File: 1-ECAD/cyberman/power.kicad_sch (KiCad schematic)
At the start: 49 parts, among them J601 S3B-ZR-SM4A-TF, U601 MAX17048G+T10, U602 BQ25896RTWR, U604 RS3221-3.3YF3, U605 DMN313DLT-7, U606 DMP1045U-7, U607 TPS62825DMQR, U608 TPS62824ADMQ, U609 MMDT2907A-7-F

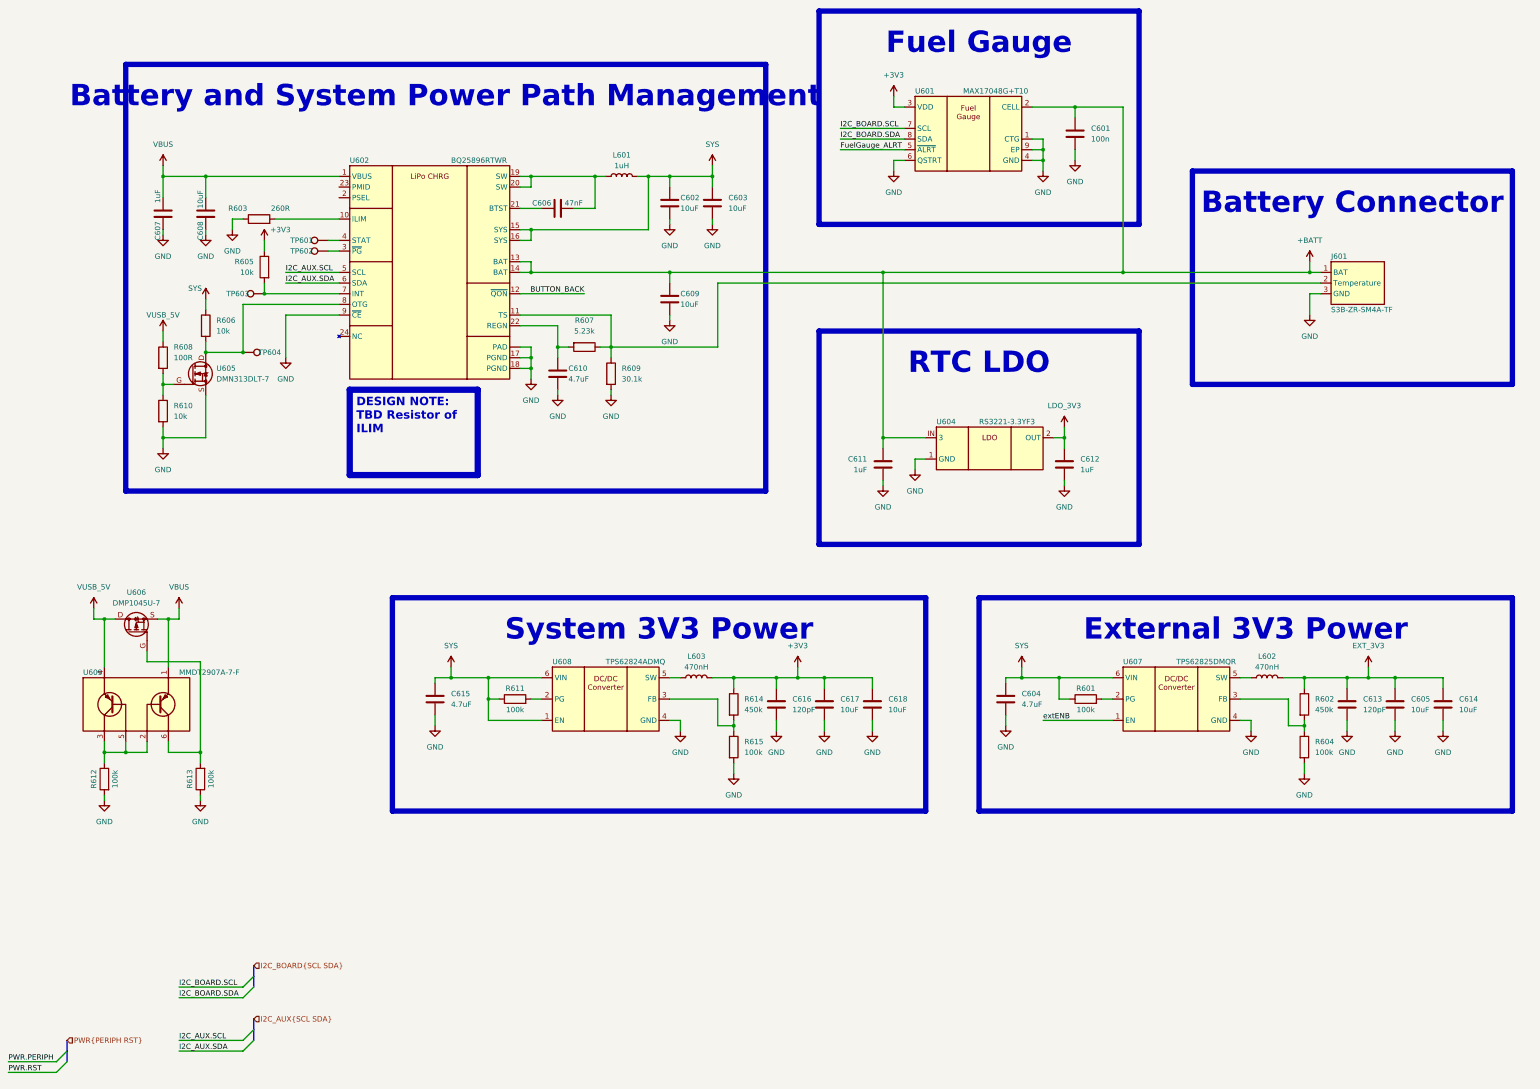
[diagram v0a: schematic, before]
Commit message: power page almost done
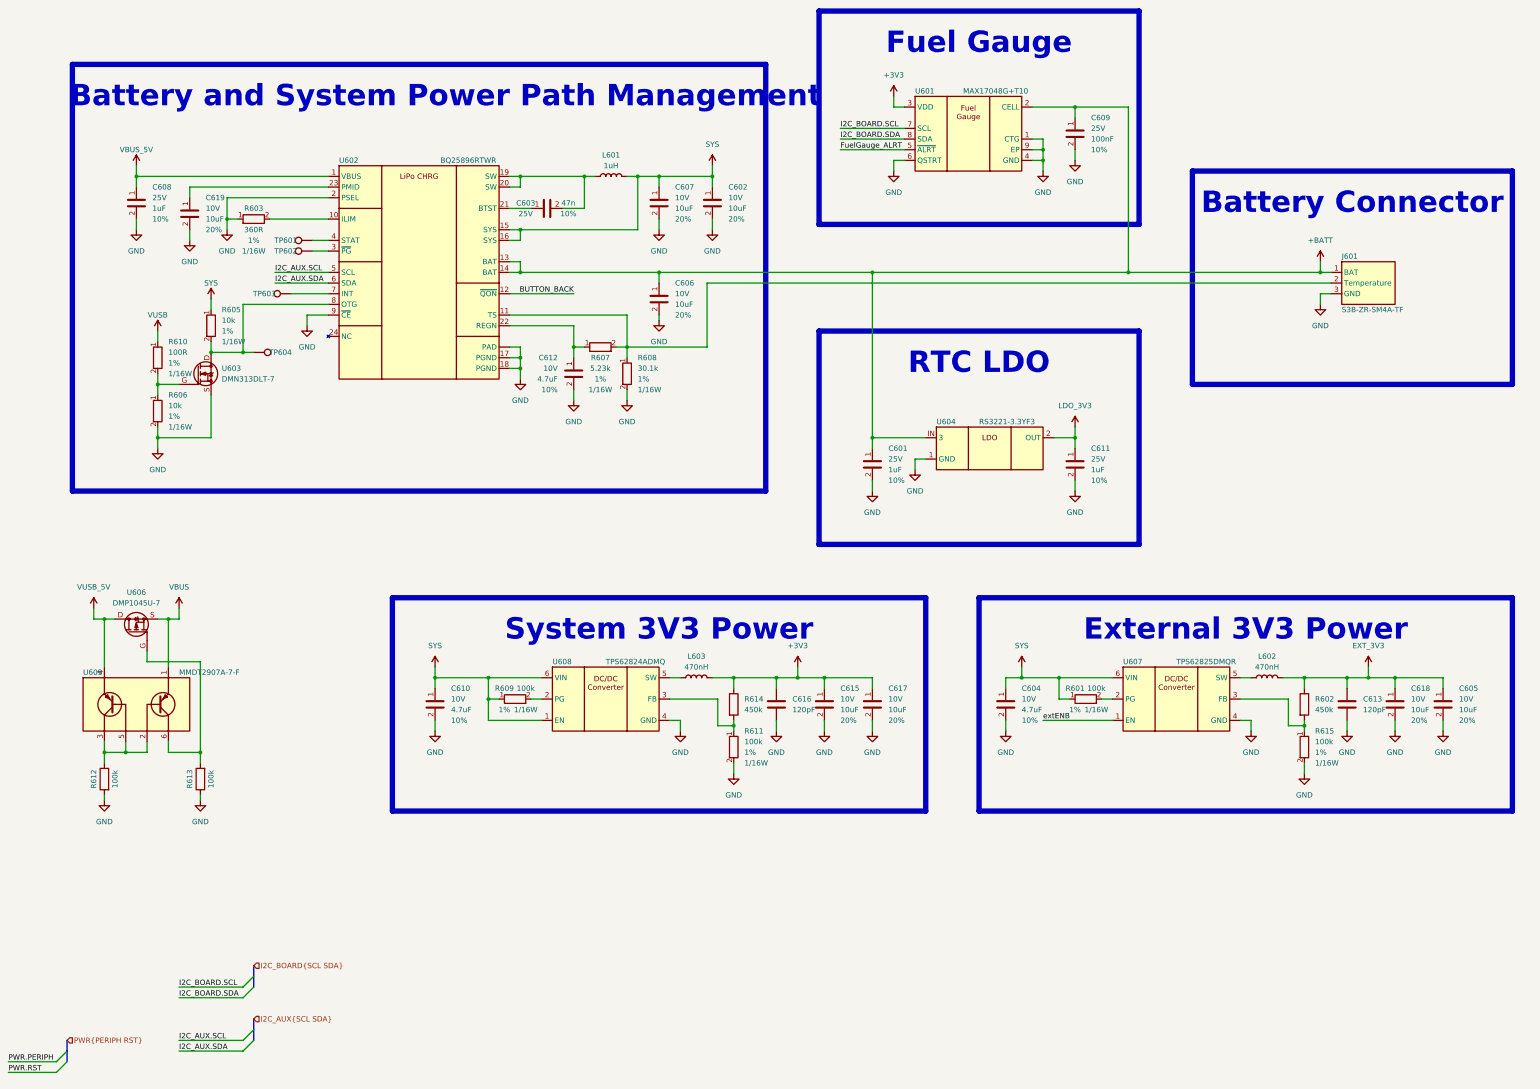
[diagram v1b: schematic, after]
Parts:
- removed C601: 100n, symbol Device:C
- removed C602, C603, C605, C608, C609, C614, C617, C618: 10uF, symbol Device:C
- removed C604, C610, C615: 4.7uF, symbol Device:C
- removed C606: 47nF, symbol Device:C
- removed C607, C611, C612: 1uF, symbol Device:C
- removed R601, R604, R611, R615: 100k, symbol Device:R
- removed R603: 260R, symbol Device:R
- removed R605, R606, R610: 10k, symbol Device:R
- removed R607: 5.23k, symbol Device:R
- removed R608: 100R, symbol Device:R
- removed R609: 30.1k, symbol Device:R
- removed U605: DMN313DLT-7, symbol 0_CI_smd:DMN313DLT-7
- added C601, C608, C611: CC0402KRX5R8BB105, 0_capacitor_smd:C_0402, symbol 0_capacitor_smd:CC0402KRX5R8BB105
- added C602, C605, C606, C607, C615, C617, C618, C619: CC0402MRX5R6BB106, 0_capacitor_smd:C_0402, symbol 0_capacitor_smd:CC0402MRX5R6BB106
- added C603: CC0402KRX7R8BB473, 0_capacitor_smd:C_0402, symbol 0_capacitor_smd:CC0402KRX7R8BB473
- added C604, C610, C612: CC0402KRX5R6BB475, 0_capacitor_smd:C_0402, symbol 0_capacitor_smd:CC0402KRX5R6BB475
- added C609: CC0402KRX7R8BB104, 0_capacitor_smd:C_0402, symbol 0_capacitor_smd:CC0402KRX7R8BB104
- added R601, R609, R611, R615: RC0402FR-07100KL, 0_resistor_smd:R_0402, symbol 0_resistor_smd:RC0402FR-07100KL
- added R603: RC0402FR-07360RL, 0_resistor_smd:R_0402, symbol 0_resistor_smd:RC0402FR-07360RL
- added R605, R606: RC0402FR-0710KL, 0_resistor_smd:R_0402, symbol 0_resistor_smd:RC0402FR-0710KL
- added R607: RC0402FR-075K23L, 0_resistor_smd:R_0402, symbol 0_resistor_smd:RC0402FR-075K23L
- added R608: RC0402FR-0730K1L, 0_resistor_smd:R_0402, symbol 0_resistor_smd:RC0402FR-0730K1L
- added R610: RC0402FR-07100RL, 0_resistor_smd:R_0402, symbol 0_resistor_smd:RC0402FR-07100RL
- added U603: DMN313DLT-7, 0_CI_smd:DMN313DLT-7, symbol 0_CI_smd:DMN313DLT-7
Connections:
- net +3V3: now also C615.1, C617.1
- net +BATT: now also C601.1, C606.1, C609.1
- net EXT_3V3: now also C605.1, C618.1
- net GND: now also U602.2 (PSEL), C601.2, C602.2, C604.2, C605.2, C606.2, C607.2, C608.2, C609.2, C610.2, C611.2, C612.2, C615.2, C617.2, C618.2, C619.2, R603.1, R606.2, R608.2, R611.2, R615.2, U603.S
- net LDO_3V3: now also C611.1
- net SYS: now also C602.1, C604.1, C607.1, C610.1, R601.1, R605.1, R609.1
- net VBUS: no longer U602.1 (VBUS)
- net at U602.10 (ILIM): now also R603.2
- net at J601.2 (Temperature), U602.11 (TS): now also R607.2, R608.1
- net at L601.1, U602.19 (SW), U602.20 (SW): now also C603.2
- net at U602.21 (BTST): now also C603.1
- net at U602.22 (REGN): now also C612.1, R607.1
- net at U602.23 (PMID): now also C619.1
- net at TP604.1, U602.8 (OTG): now also R605.2, U603.D
- net at R602.2, U607.3 (FB): now also R615.1
- net at U607.2 (PG): now also R601.2
- net at R614.2, U608.3 (FB): now also R611.1
- net at U608.2 (PG): now also R609.2
- new net: R606.1, R610.2, U603.G
- new net VBUS_5V: C608.1, U602.1 (VBUS)
- new net VUSB: R610.1
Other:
- moved on the sheet: J601, L601, TP601, TP602, TP603, TP604, U602

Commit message: new footprints
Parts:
- removed C613, C616: 120pF, symbol Device:C
- removed R602, R614: 450k, symbol Device:R
- added C614, C616: CC0402KRX7R9BB121, 0_capacitor_smd:C_0402, symbol 0_capacitor_smd:CC0402KRX7R9BB121
- added R604, R614: RC0402FR-07453KL, 0_resistor_smd:R_0402, symbol 0_resistor_smd:RC0402FR-07453KL
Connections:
- net +3V3: now also C614.1, R604.1
- net EXT_3V3: now also C616.1, R614.1
- net GND: now also C614.2, C616.2
- net at R615.1, U607.3 (FB): now also R614.2
- net at R611.1, U608.3 (FB): now also R604.2

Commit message: power page close
siuuuuuuuuuuuu
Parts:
- removed L601: 1uH, symbol Device:L
- removed L602, L603: 470nH, symbol Device:L
- removed R603: RC0402FR-07360RL, 0_resistor_smd:R_0402, symbol 0_resistor_smd:RC0402FR-07360RL
- removed R612, R613: 100k, symbol Device:R
- removed TP601, TP602, TP603, TP604: TestPoint, symbol Connector:TestPoint
- removed U606: DMP1045U-7, symbol 0_CI_smd:DMP1045U-7
- removed U609: MMDT2907A-7-F, 0_CI_smd:MMDT2907A-7-F, symbol 0_CI_smd:MMDT2907A-7-F
- added L601: DFE252012P-1R0M=P2, 0_inductor_smd:DFE252012P-1R0M=P2, symbol 0_inductor_smd:DFE252012P-1R0M=P2
- added L602: MLP2012HR47MT0S1, 0_inductor_smd:MLP2012HR47MT0S1, symbol 0_inductor_smd:MLP2012HR47MT0S1
- added L603: LQM2MPNR47MGHL, 0_inductor_smd:LQM2MPNR47MGHL, symbol 0_inductor_smd:LQM2MPNR47MGHL
- added R601: RC0402FR-07470RL, 0_resistor_smd:R_0402, symbol 0_resistor_smd:RC0402FR-07470RL
- added R602, R613: RC0402FR-0710KL, 0_resistor_smd:R_0402, symbol 0_resistor_smd:RC0402FR-0710KL
- added R615, R616: RC0402FR-07100KL, 0_resistor_smd:R_0402, symbol 0_resistor_smd:RC0402FR-07100KL
- added TP601: STAT, 0_testpoint:TestPoint_Pad_D0.5mm_Front, symbol 0_test_points:testpoint
- added TP602: PG, 0_testpoint:TestPoint_Pad_D0.5mm_Front, symbol 0_test_points:testpoint
- added TP603: TEMP, 0_testpoint:TestPoint_Pad_D0.5mm_Front, symbol 0_test_points:testpoint
- added TP604: OTG, 0_testpoint:TestPoint_Pad_D0.5mm_Front, symbol 0_test_points:testpoint
- added TP605, TP607: 5V1, 0_testpoint:TestPoint_Pad_D0.5mm_Front, symbol 0_test_points:testpoint
- added TP606: 3V31, 0_testpoint:TestPoint_Pad_D0.5mm_Front, symbol 0_test_points:testpoint
- added TP608: 3V32, 0_testpoint:TestPoint_Pad_D0.5mm_Front, symbol 0_test_points:testpoint
- added TP609: GND1, 0_testpoint:TestPoint_Pad_D0.5mm_Front, symbol 0_test_points:testpoint
- added TP610: GND2, 0_testpoint:TestPoint_Pad_D0.5mm_Front, symbol 0_test_points:testpoint
- added TP611: GND3, 0_testpoint:TestPoint_Pad_D0.5mm_Front, symbol 0_test_points:testpoint
- added TP612: BAT1, 0_testpoint:TestPoint_Pad_D0.5mm_Front, symbol 0_test_points:testpoint
- added TP613: EXT3V31, 0_testpoint:TestPoint_Pad_D0.5mm_Front, symbol 0_test_points:testpoint
- added TP614: GND4, 0_testpoint:TestPoint_Pad_D0.5mm_Front, symbol 0_test_points:testpoint
- added TP615: BAT2, 0_testpoint:TestPoint_Pad_D0.5mm_Front, symbol 0_test_points:testpoint
- added TP616: EXT3V32, 0_testpoint:TestPoint_Pad_D0.5mm_Front, symbol 0_test_points:testpoint
- added TP617: SYS1, 0_testpoint:TestPoint_Pad_D0.5mm_Front, symbol 0_test_points:testpoint
- added TP618: LDO1, 0_testpoint:TestPoint_Pad_D0.5mm_Front, symbol 0_test_points:testpoint
- added TP619: SYS2, 0_testpoint:TestPoint_Pad_D0.5mm_Front, symbol 0_test_points:testpoint
- added TP620: LDO2, 0_testpoint:TestPoint_Pad_D0.5mm_Front, symbol 0_test_points:testpoint
- added U607: DMP1045U-7, 0_CI_smd:DMP1045U-7, symbol 0_CI_smd:DMP1045U-7
- added U608: MMDT2907A-7-F, 0_CI_smd:MMDT2907A-7-F, symbol 0_CI_smd:MMDT2907A-7-F
- renumbered C609 to C601, C608 to C602, C607 to C603, C602 to C604, C603 to C605, C619 to C606, C606 to C607, C612 to C608, C601 to C609, C611 to C610, C610 to C611, C614 to C612, C615 to C613, C617 to C614, C604 to C615, C618 to C617, C605 to C618, R605 to R603, R607 to R604, R610 to R605, R608 to R606, R606 to R607, R609 to R608, R601 to R609, R604 to R610, R614 to R611, R611 to R612, R615 to R614, U608 to U605, U607 to U606
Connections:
- net BUTTON_BACK is gone; now on net PWR.RST: U602.12 (~{QON})
- net extENB is gone; now on net PWR.PERIPH: U606.1 (EN)
- net +3V3: now also L602.2, R602.1, R613.2, TP606.1, TP608.1
- net EXT_3V3: now also L603.2, TP613.1, TP616.1
- net GND: now also R601.1, R615.2, R616.2, TP609.1, TP610.1, TP611.1, TP614.1
- net LDO_3V3: now also TP618.1, TP620.1
- net PWR.PERIPH: now also R613.1
- net SYS: now also L601.2, TP617.1, TP619.1
- net VBUS_5V: now also TP605.1, TP607.1, U607.S, U608.1
- net VUSB: now also U607.D, U608.4
- net at J601.2 (Temperature), R604.2, R606.1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: now also TP603.1
- net at U602.10 (ILIM): now also R601.2
- net at C605.2, U602.19 (SW), U602.20 (SW): now also L601.1
- net at U602.3 (~{PG}): now also TP602.1
- net at U602.4 (STAT): now also TP601.1
- net PWR.INT: now reaches U602.7 (INT)
- net PWR.INT: now also R602.2
- net at R603.2, U602.8 (OTG), U603.D: now also TP604.1
- net at U606.5 (SW): now also L603.1
- net at U605.5 (SW): now also L602.1
- net +BATT renamed +BAT
- net +BAT: now also TP612.1, TP615.1
- net FuelGauge_ALRT renamed FG_ALRT
- new net: R616.1, U607.G, U608.6
- new net: R615.1, U608.2, U608.3, U608.5
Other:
- note added: "Switch"
- note added: "Test Points"
- moved on the sheet: C611, C612, C613, C614, C615, C616, C617, C618, R603, R605, R607, R608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
